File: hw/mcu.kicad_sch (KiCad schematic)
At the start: 41 parts, among them J2 FPC, J3 Wisevision N114-2413THBIG01-H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, J4 Prog/debug, Q3 AO3401A, Q4 2N7002, Q5 2N7002, SW1 SW_Push_Shielded, SW2 SW_Push_Shielded, SW3 SW_Push_Shielded, SW8 Reset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

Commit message: Routing in progress.
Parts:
- removed Q5: 2N7002, Package_TO_SOT_SMD:SOT-23, symbol Transistor_FET:2N7002
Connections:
- net BUTTON_SW2: now also U5.24 (PC4); no longer U5.11 (PC3)
- net BUTTON_SW3: now also U5.25 (PC5); no longer U5.10 (PC2)
- net BUTTON_SW4_Down: now also U5.55 (PB3); no longer U5.51 (PC10)
- net BUTTON_SW4_Left: now also U5.51 (PC10); no longer U5.52 (PC11)
- net BUTTON_SW4_Push: now also U5.52 (PC11); no longer U5.55 (PB3)
- net BUTTON_SW4_Right: now also U5.50 (PA15); no longer U5.53 (PC12)
- net BUTTON_SW4_Up: now also U5.53 (PC12); no longer U5.50 (PA15)
- net BUTTON_WAKE: now also SW1.2; no longer SW1.1
- net BUZZER: now also U5.59 (PB7); no longer U5.21 (PA5)
- net EXT_PA10: now also J2.1 (Pin_1); no longer J2.5 (Pin_5)
- net EXT_PA8: now also J2.4 (Pin_4); no longer J2.1 (Pin_1)
- net LCD_SDAT: now also J2.5 (Pin_5); no longer J2.4 (Pin_4)
- net VDD: now also SW1.1; no longer SW1.2
- net VMEAS_GND: now reaches U5.58 (PB6)
- net VMEAS_GND: now also R20.1
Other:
- note added: "Battery/charging voltage measurement. --> Set VMEAS_GND to 0 to measure. --> Turn off ADC input when not measuring."
- note added: "Crystal @ LSE LCD @ SPI2 half-duplex QSPI Flash @ QSPI Bank 1 Buzzer @ TIM4 Channel 2 LCD Backlight @ GPIO or TIM3 Channel 1 Note: PC13 can serve as RTC calibration output."
- note removed: "Battery/charging voltage measurement when LCD backlight is on. --> Turn off ADC input when LCD backlight is off."
- note removed: "Crystal @ LSE LCD @ SPI2 half-duplex QSPI Flash @ QSPI Bank 1 Buzzer @ TIM2 Channel 1 LCD Backlight @ GPIO or TIM3 Channel 1 Note: PC13 can serve as RTC calibration output."

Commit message: Routed.
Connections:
- net LCD_BL: now also U5.38 (PC7); no longer U5.37 (PC6)
- net LCD_nPWR: now also U5.37 (PC6); no longer U5.38 (PC7)
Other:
- note added: "Crystal @ LSE LCD @ SPI2 half-duplex QSPI Flash @ QSPI Bank 1 Buzzer @ TIM4 Channel 2 LCD Backlight @ GPIO or TIM3 Channel 2 Note: PC13 can serve as RTC calibration output."
- note removed: "Crystal @ LSE LCD @ SPI2 half-duplex QSPI Flash @ QSPI Bank 1 Buzzer @ TIM4 Channel 2 LCD Backlight @ GPIO or TIM3 Channel 1 Note: PC13 can serve as RTC calibration output."
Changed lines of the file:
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@@
 		)
 	)
-	(text "Crystal        @ LSE\nLCD           @ SPI2 half-duplex\nQSPI Flash    @ QSPI Bank 1\nBuzzer        @ TIM4 Channel 2\nLCD Backlight @ GPIO or TIM3 Channel 1\n\nNote: PC13 can serve as RTC calibration output."
+	(text "Crystal        @ LSE\nLCD           @ SPI2 half-duplex\nQSPI Flash    @ QSPI Bank 1\nBuzzer        @ TIM4 Channel 2\nLCD Backlight @ GPIO or TIM3 Channel 2\n\nNote: PC13 can serve as RTC calibration output."
 		(exclude_from_sim no)
 		(at 15.24 118.11 0)
@@
 		)
 	)
+	(label "LCD_BL"
+		(at 52.07 74.93 0)
+		(effects
+			(font
+				(size 1.27 1.27)
+			)
+			(justify left bottom)
+		)
+	)
 	(label "FLASH_SCK"
 		(at 111.76 105.41 180)
@@
 		)
 	)
-	(label "LCD_nPWR"
-		(at 52.07 74.93 0)
-		(effects
-			(font
-				(size 1.27 1.27)
-			)
-			(justify left bottom)
-		)
-	)
 	(label "BUTTON_SW4_Up"
 		(at 179.07 148.59 0)
@@
 		)
 	)
+	(label "LCD_nPWR"
+		(at 52.07 72.39 0)
+		(effects
+			(font
+				(size 1.27 1.27)
+			)
+			(justify left bottom)
+		)
+	)
 	(label "SWDIO"
 		(at 109.22 69.85 180)
@@
 		)
 	)
-	(label "LCD_BL"
-		(at 52.07 72.39 0)
-		(effects
-			(font
-				(size 1.27 1.27)
-			)
-			(justify left bottom)
-		)
-	)

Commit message: Supposedly finished.
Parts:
- added TP4: Ground, TestPoint:TestPoint_Pad_D1.0mm, symbol Connector:TestPoint
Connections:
- net GND: now also TP4.1
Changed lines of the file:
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@@
+	)
+	(symbol
+		(lib_id "Connector:TestPoint")
+		(at 17.78 88.9 0)
+		(unit 1)
+		(exclude_from_sim no)
+		(in_bom yes)
+		(on_board yes)
+		(dnp no)
+		(fields_autoplaced yes)
+		(property "Reference" "TP4"
+			(at 20.32 84.3279 0)
+			(effects
+				(font
+					(size 1.27 1.27)
+				)
+				(justify left)
+			)
+		)
+		(property "Value" "Ground"
+			(at 20.32 86.8679 0)
+			(effects
+				(font
+					(size 1.27 1.27)
+				)
+				(justify left)
+			)
+		)
+		(property "Footprint" "TestPoint:TestPoint_Pad_D1.0mm"
+			(at 22.86 88.9 0)
+			(effects
+				(font
+					(size 1.27 1.27)
+				)
+				(hide yes)
+			)
+		)
+		(property "Datasheet" "~"
+			(at 22.86 88.9 0)
+			(effects
+				(font
+					(size 1.27 1.27)
+				)
+				(hide yes)
+			)
+		)
+		(property "Description" "test point"
+			(at 17.78 88.9 0)
+			(effects
+				(font
+					(size 1.27 1.27)
+				)
+				(hide yes)
+			)
+		)
+		(pin "1"
+		)
+		(instances
+			(project "sem18"
+				(path "/d844aefd-19cf-4889-9465-41f3f1184bf3/32e28d38-9cf3-4528-9413-17cfc341889c"
+					(reference "TP4")
+					(unit 1)
+				)
+			)
+		)
 	)
 	(symbol
@@
 					(unit 1)
 				)
+			)
+		)
+	)
+	(symbol
+		(lib_id "power:GND")
+		(at 17.78 88.9 0)
+		(unit 1)
+		(exclude_from_sim no)
+		(in_bom yes)
+		(on_board yes)
+		(dnp no)
+		(fields_autoplaced yes)
+		(property "Reference" "#PWR043"
+			(at 17.78 95.25 0)
+			(effects
+				(font
+					(size 1.27 1.27)
+				)
+				(hide yes)
+			)
+		)
+		(property "Value" "GND"
+			(at 17.78 93.98 0)
+			(effects
+				(font
+					(size 1.27 1.27)
+				)
+			)
+		)
+		(property "Footprint" ""
+			(at 17.78 88.9 0)
+			(effects
+				(font
+					(size 1.27 1.27)
+				)
+				(hide yes)
+			)
+		)
+		(property "Datasheet" ""
+			(at 17.78 88.9 0)
+			(effects
+				(font
+					(size 1.27 1.27)
+				)
+				(hide yes)
+			)
+		)
+		(property "Description" "Power symbol creates a global label with name \"GND\" , ground"
+			(at 17.78 88.9 0)
+			(effects
+				(font
+					(size 1.27 1.27)
+				)
+				(hide yes)
+			)
+		)
+		(pin "1"
+		)
+		(instances
+			(project "sem18"
+				(path "/d844aefd-19cf-4889-9465-41f3f1184bf3/32e28d38-9cf3-4528-9413-17cfc341889c"
+					(reference "#PWR043")
+					(unit 1)
+				)

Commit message: Works.
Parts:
- C11, C12: value TBD -> 20pF
- R15: value 1k -> 100
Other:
- note removed: "<-- This might need to be changed..."
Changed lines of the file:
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@@
 		)
 	)
-	(text "<-- This might need to be changed..."
-		(exclude_from_sim no)
-		(at 172.72 167.132 0)
-		(effects
-			(font
-				(size 1.27 1.27)
-			)
-		)
-	)
 	(text "Pinout compatible with SEM-karifa-2023.\nWatch out for the operating voltage (3.0V)!"
 		(exclude_from_sim no)
@@
 			)
 		)
-		(property "Value" "1k"
+		(property "Value" "100"
 			(at 149.86 167.6399 0)
 			(effects
@@
 			)
 		)
-		(property "Value" "TBD"
+		(property "Value" "20pF"
 			(at 27.94 105.4099 0)
 			(effects
@@
 			)
 		)
-		(property "Value" "TBD"
+		(property "Value" "20pF"
 			(at 40.64 105.4099 0)
 			(effects

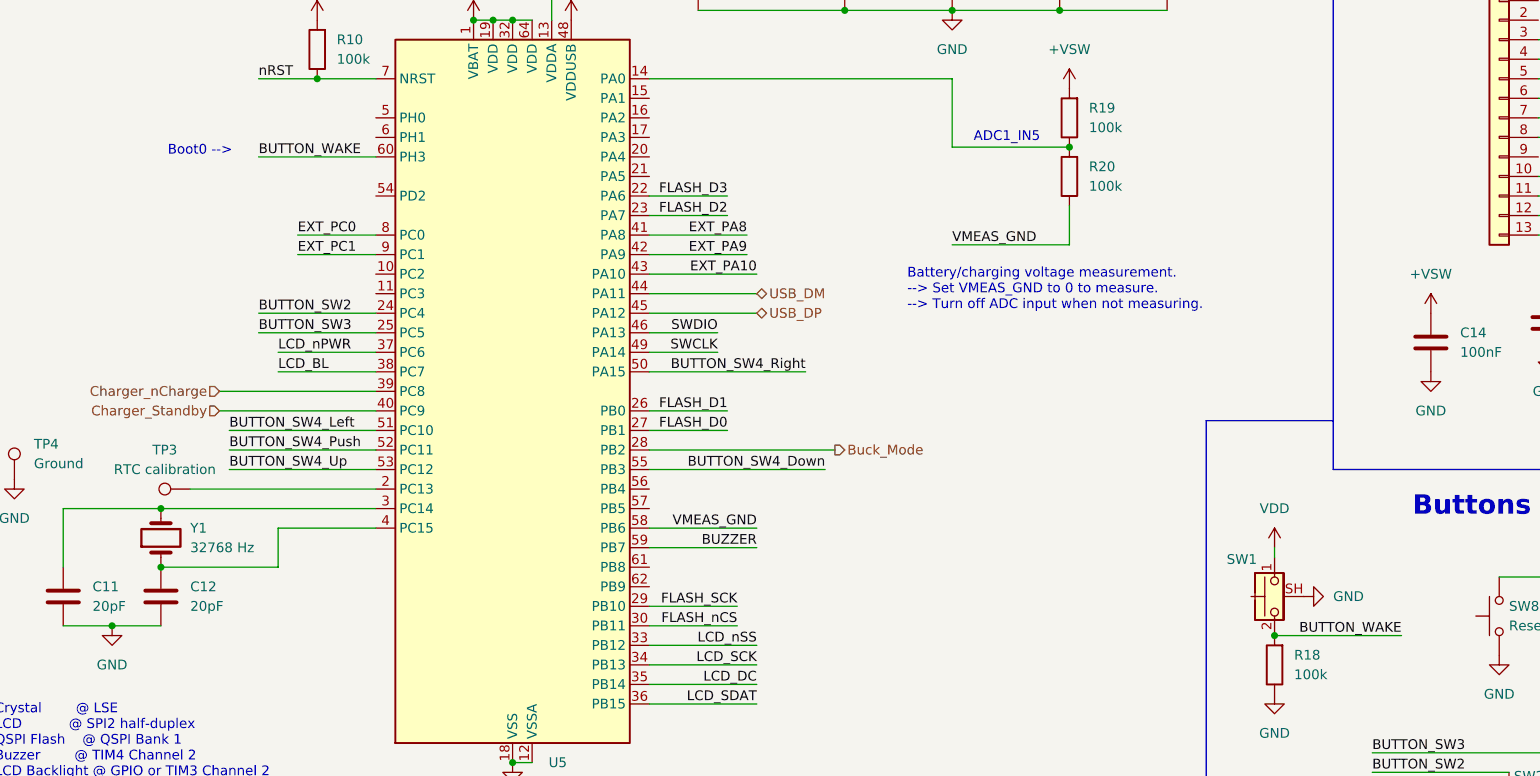
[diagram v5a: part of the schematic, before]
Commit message: Changed naming of the upper left button.
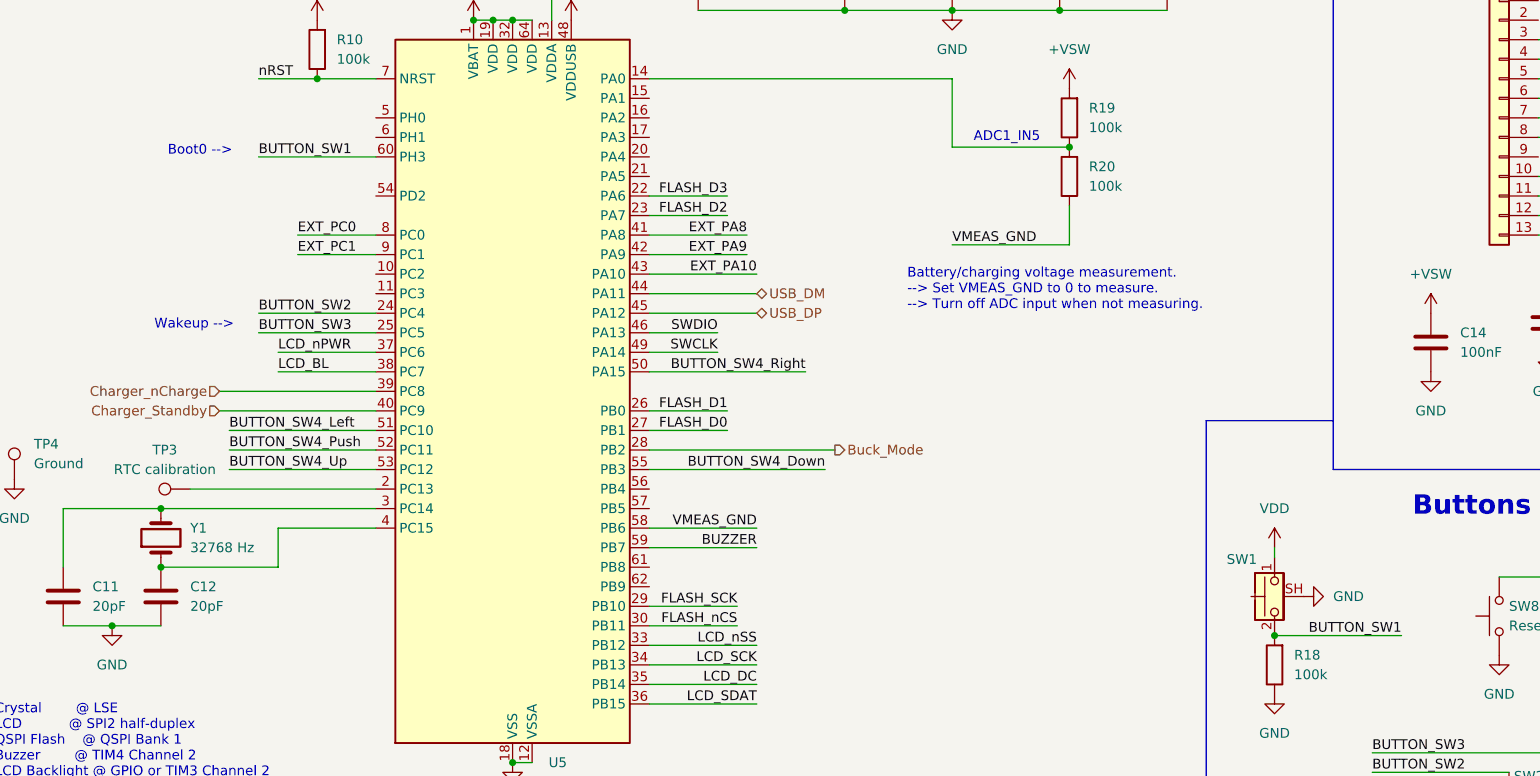
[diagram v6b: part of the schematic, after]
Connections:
- net BUTTON_WAKE renamed BUTTON_SW1
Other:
- note added: "Wakeup -->"
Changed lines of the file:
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@@
+		)
+	)
+	(text "Wakeup -->"
+		(exclude_from_sim no)
+		(at 41.148 68.834 0)
+		(effects
+			(font
+				(size 1.27 1.27)
+			)
 		)
 	)
@@
 		)
 	)
-	(label "BUTTON_WAKE"
+	(label "BUTTON_SW1"
 		(at 49.53 46.99 0)
 		(effects
@@
 		)
 	)
-	(label "BUTTON_WAKE"
+	(label "BUTTON_SW1"
 		(at 198.12 109.22 180)
 		(effects
